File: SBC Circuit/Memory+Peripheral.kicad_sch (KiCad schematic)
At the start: 15 parts, among them U2 68681, U4 MCM6206CP, U5 28C256, U6 MCM6206CP, U7 28C256

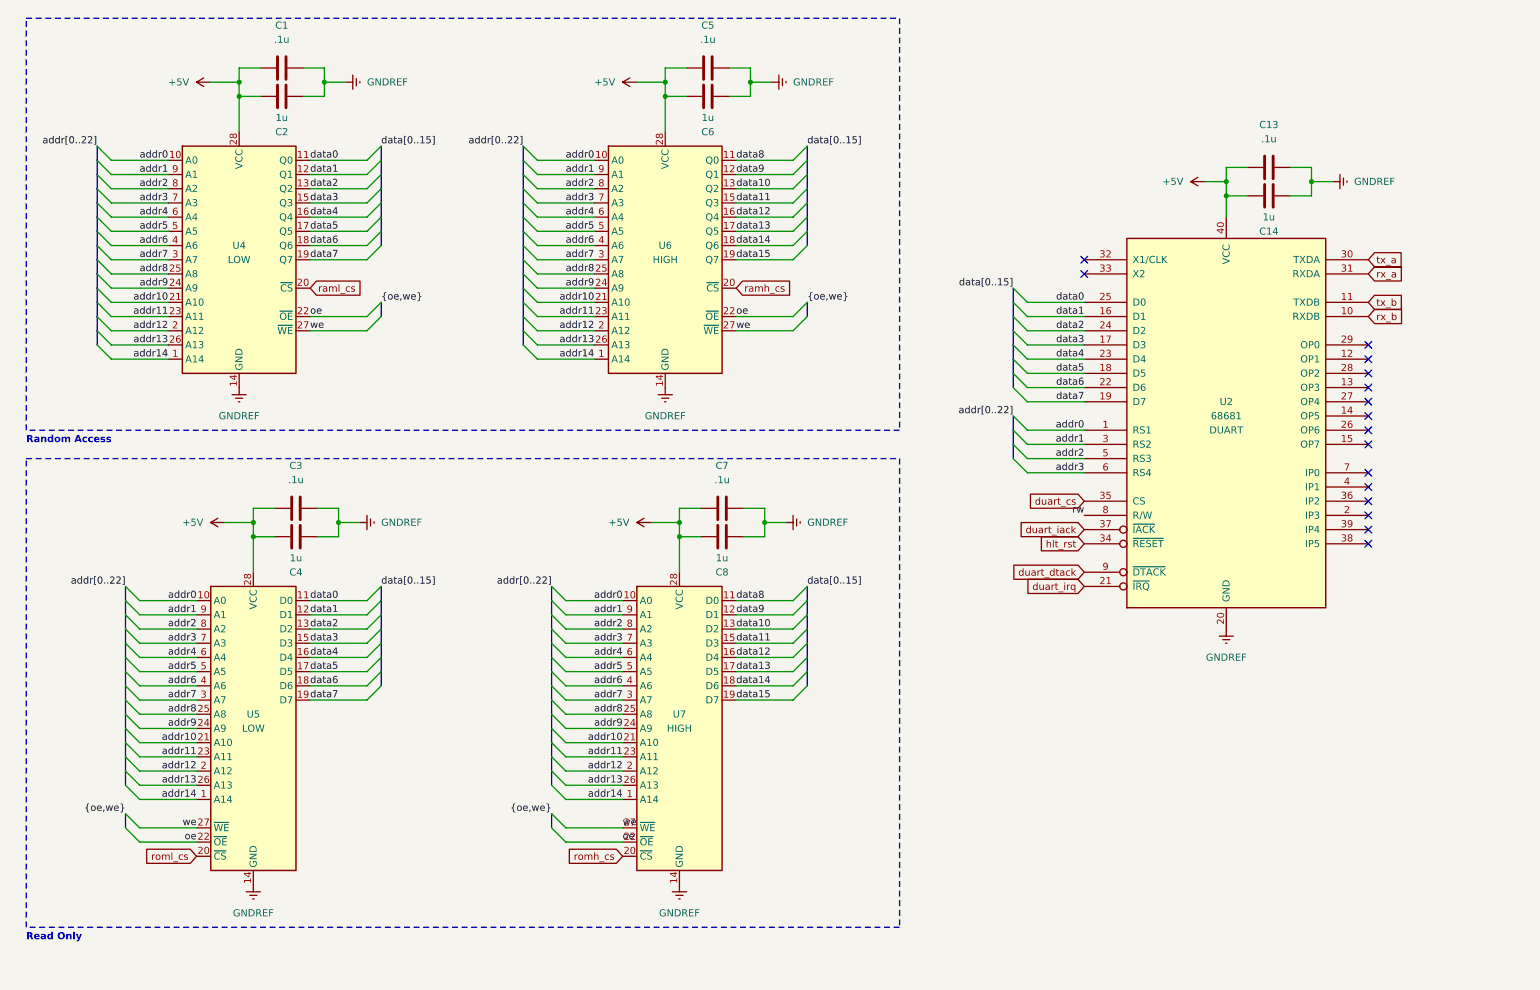
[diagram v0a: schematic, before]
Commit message: Add peripheral headers to schematic
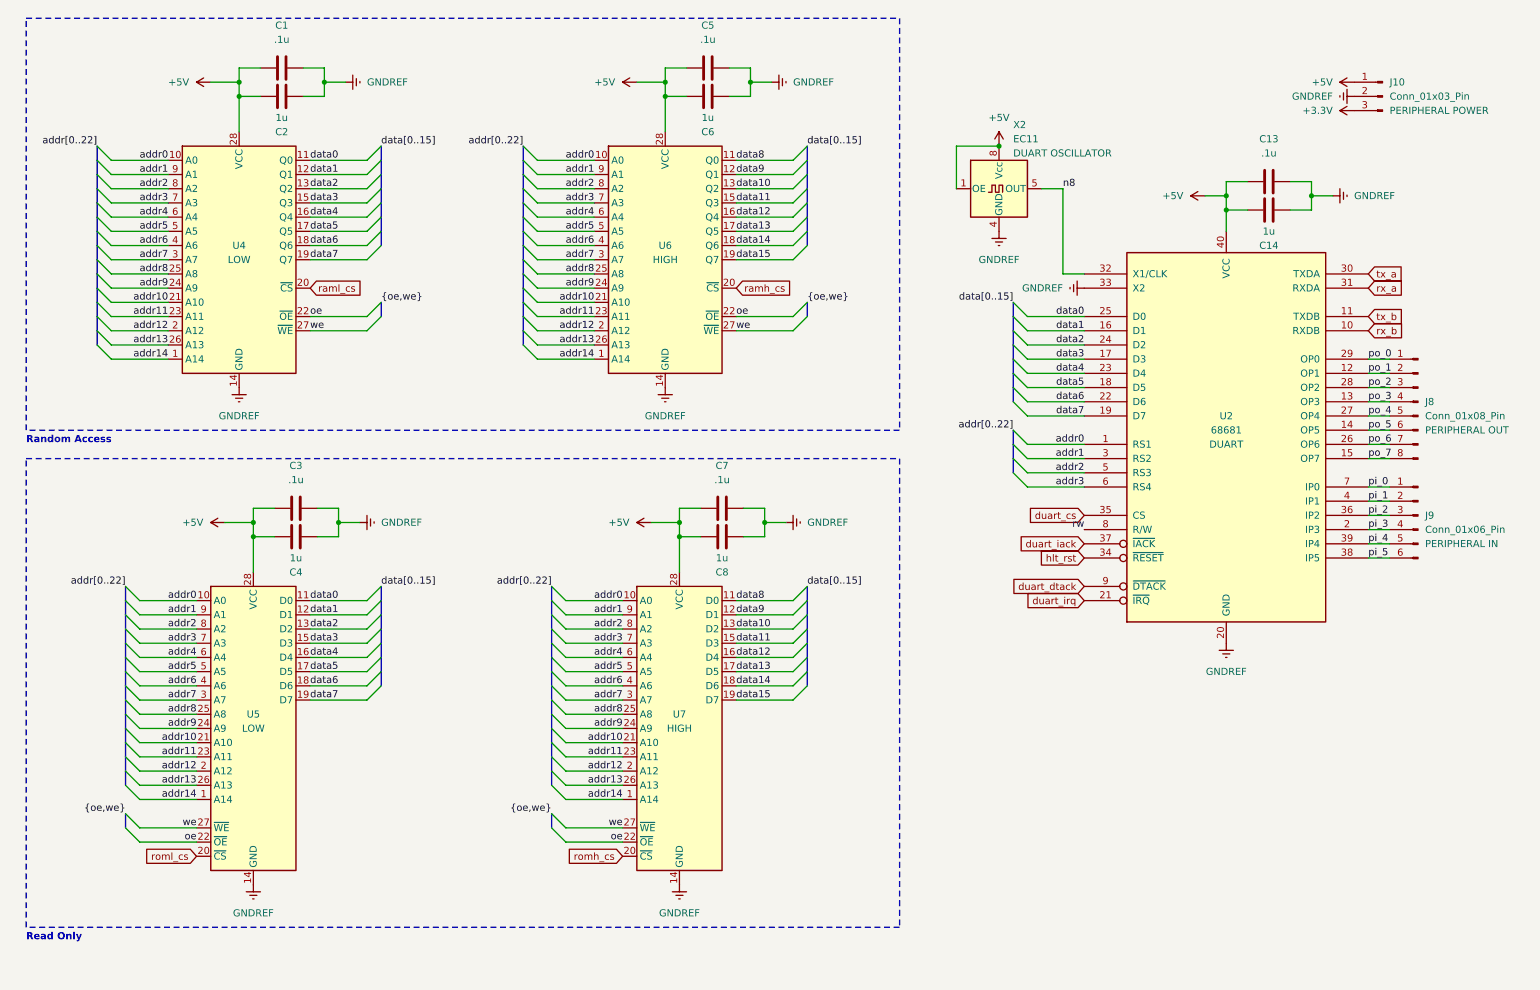
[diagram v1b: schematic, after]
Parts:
- added J10: Conn_01x03_Pin, symbol Connector:Conn_01x03_Pin
- added J8: Conn_01x08_Pin, symbol Connector:Conn_01x08_Pin
- added J9: Conn_01x06_Pin, symbol Connector:Conn_01x06_Pin
- added X2: EC11, Oscillator:Oscillator_SeikoEpson_SG-8002DC, symbol Oscillator:EC11
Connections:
- net +5V: now also J10.1 (Pin_1), X2.1 (OE), X2.8 (Vcc)
- net GNDREF: now also U2.33 (X2), J10.2 (Pin_2), X2.4 (GND)
- net po_1: now reaches U2.12 (OP1)
- net po_1: now also J8.2 (Pin_2)
- net po_3: now reaches U2.13 (OP3)
- net po_3: now also J8.4 (Pin_4)
- net po_5: now reaches U2.14 (OP5)
- net po_5: now also J8.6 (Pin_6)
- net po_7: now reaches U2.15 (OP7)
- net po_7: now also J8.8 (Pin_8)
- net pi_3: now reaches U2.2 (IP3)
- net pi_3: now also J9.4 (Pin_4)
- net po_6: now reaches U2.26 (OP6)
- net po_6: now also J8.7 (Pin_7)
- net po_4: now reaches U2.27 (OP4)
- net po_4: now also J8.5 (Pin_5)
- net po_2: now reaches U2.28 (OP2)
- net po_2: now also J8.3 (Pin_3)
- net po_0: now reaches U2.29 (OP0)
- net po_0: now also J8.1 (Pin_1)
- net n8: now reaches U2.32 (X1/CLK)
- net n8: now also X2.5 (OUT)
- net pi_2: now reaches U2.36 (IP2)
- net pi_2: now also J9.3 (Pin_3)
- net pi_5: now reaches U2.38 (IP5)
- net pi_5: now also J9.6 (Pin_6)
- net pi_4: now reaches U2.39 (IP4)
- net pi_4: now also J9.5 (Pin_5)
- net pi_1: now reaches U2.4 (IP1)
- net pi_1: now also J9.2 (Pin_2)
- net pi_0: now reaches U2.7 (IP0)
- net pi_0: now also J9.1 (Pin_1)
- new net +3.3V: J10.3 (Pin_3)
- no-connect marks 16 -> 0
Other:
- moved on the sheet: C13, C14, U2

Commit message: Reannotate schematic
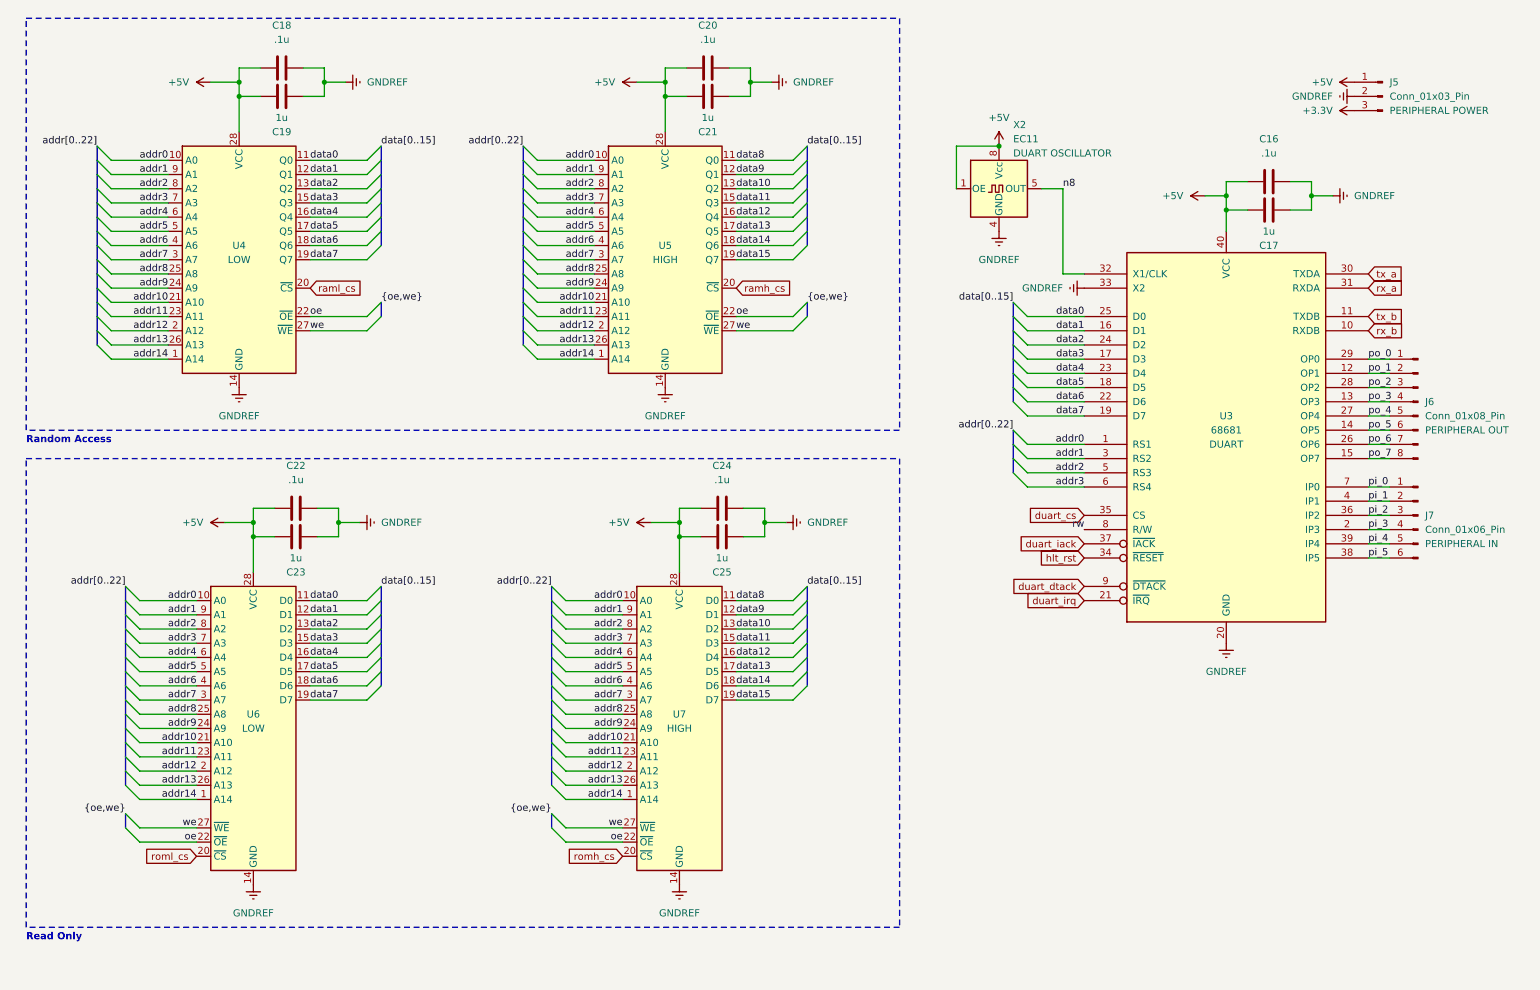
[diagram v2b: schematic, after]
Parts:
- renumbered C13 to C16, C14 to C17, C1 to C18, C2 to C19, C5 to C20, C6 to C21, C3 to C22, C4 to C23, C7 to C24, C8 to C25, J10 to J5, J8 to J6, J9 to J7, U2 to U3, U6 to U5, U5 to U6
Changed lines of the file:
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@@
   (symbol (lib_id "Device:C") (at 64.77 114.3 90) (mirror x) (unit 1)
     (in_bom yes) (on_board yes) (dnp no)
-    (property "Reference" "C4" (at 64.77 120.65 90)
+    (property "Reference" "C23" (at 64.77 120.65 90)
       (effects (font (size 1.27 1.27)))
     )
@@
       (project "SBC Circuit"
         (path "/3db026c4-f98d-4c94-ab2a-d9924b8daebe/58631114-4a93-4344-80be-9965735307cd"
-          (reference "C4") (unit 1)
+          (reference "C23") (unit 1)
         )
       )
@@
   (symbol (lib_id "Device:C") (at 64.77 109.22 90) (unit 1)
     (in_bom yes) (on_board yes) (dnp no) (fields_autoplaced)
-    (property "Reference" "C3" (at 64.77 101.6 90)
+    (property "Reference" "C22" (at 64.77 101.6 90)
       (effects (font (size 1.27 1.27)))
     )
@@
       (project "SBC Circuit"
         (path "/3db026c4-f98d-4c94-ab2a-d9924b8daebe/58631114-4a93-4344-80be-9965735307cd"
-          (reference "C3") (unit 1)
+          (reference "C22") (unit 1)
         )
       )
@@
   (symbol (lib_id "Memory_RAM:MCM6206CP") (at 130.81 64.77 0) (unit 1)
     (in_bom yes) (on_board yes) (dnp no)
-    (property "Reference" "U6" (at 130.81 62.23 0)
+    (property "Reference" "U5" (at 130.81 62.23 0)
       (effects (font (size 1.27 1.27)))
     )
@@
       (project "SBC Circuit"
         (path "/3db026c4-f98d-4c94-ab2a-d9924b8daebe/58631114-4a93-4344-80be-9965735307cd"
-          (reference "U6") (unit 1)
+          (reference "U5") (unit 1)
         )
       )
@@
   (symbol (lib_id "Device:C") (at 238.76 50.8 90) (unit 1)
     (in_bom yes) (on_board yes) (dnp no) (fields_autoplaced)
-    (property "Reference" "C13" (at 238.76 43.18 90)
+    (property "Reference" "C16" (at 238.76 43.18 90)
       (effects (font (size 1.27 1.27)))
     )
@@
       (project "SBC Circuit"
         (path "/3db026c4-f98d-4c94-ab2a-d9924b8daebe/58631114-4a93-4344-80be-9965735307cd"
-          (reference "C13") (unit 1)
+          (reference "C16") (unit 1)
         )
       )
@@
   (symbol (lib_id "Device:C") (at 238.76 55.88 90) (mirror x) (unit 1)
     (in_bom yes) (on_board yes) (dnp no)
-    (property "Reference" "C14" (at 238.76 62.23 90)
+    (property "Reference" "C17" (at 238.76 62.23 90)
       (effects (font (size 1.27 1.27)))
     )
@@
       (project "SBC Circuit"
         (path "/3db026c4-f98d-4c94-ab2a-d9924b8daebe/58631114-4a93-4344-80be-9965735307cd"
-          (reference "C14") (unit 1)
+          (reference "C17") (unit 1)
         )
       )
@@
   (symbol (lib_id "Device:C") (at 62.23 35.56 90) (mirror x) (unit 1)
     (in_bom yes) (on_board yes) (dnp no)
-    (property "Reference" "C2" (at 62.23 41.91 90)
+    (property "Reference" "C19" (at 62.23 41.91 90)
       (effects (font (size 1.27 1.27)))
     )
@@
       (project "SBC Circuit"
         (path "/3db026c4-f98d-4c94-ab2a-d9924b8daebe/58631114-4a93-4344-80be-9965735307cd"
-          (reference "C2") (unit 1)
+          (reference "C19") (unit 1)
         )
       )
@@
   (symbol (lib_id "Device:C") (at 140.97 114.3 90) (mirror x) (unit 1)
     (in_bom yes) (on_board yes) (dnp no)
-    (property "Reference" "C8" (at 140.97 120.65 90)
+    (property "Reference" "C25" (at 140.97 120.65 90)
       (effects (font (size 1.27 1.27)))
     )
@@
       (project "SBC Circuit"
         (path "/3db026c4-f98d-4c94-ab2a-d9924b8daebe/58631114-4a93-4344-80be-9965735307cd"
-          (reference "C8") (unit 1)
+          (reference "C25") (unit 1)
         )
       )
@@
   (symbol (lib_id "Device:C") (at 140.97 109.22 90) (unit 1)
     (in_bom yes) (on_board yes) (dnp no) (fields_autoplaced)
-    (property "Reference" "C7" (at 140.97 101.6 90)
+    (property "Reference" "C24" (at 140.97 101.6 90)
       (effects (font (size 1.27 1.27)))
     )
@@
       (project "SBC Circuit"
         (path "/3db026c4-f98d-4c94-ab2a-d9924b8daebe/58631114-4a93-4344-80be-9965735307cd"
-          (reference "C7") (unit 1)
+          (reference "C24") (unit 1)
         )
       )
@@
   (symbol (lib_id "Device:C") (at 138.43 35.56 90) (mirror x) (unit 1)
     (in_bom yes) (on_board yes) (dnp no)
-    (property "Reference" "C6" (at 138.43 41.91 90)
+    (property "Reference" "C21" (at 138.43 41.91 90)
       (effects (font (size 1.27 1.27)))
     )
@@
       (project "SBC Circuit"
         (path "/3db026c4-f98d-4c94-ab2a-d9924b8daebe/58631114-4a93-4344-80be-9965735307cd"
-          (reference "C6") (unit 1)
+          (reference "C21") (unit 1)
         )
       )
@@
   (symbol (lib_id "Device:C") (at 62.23 30.48 90) (unit 1)
     (in_bom yes) (on_board yes) (dnp no) (fields_autoplaced)
-    (property "Reference" "C1" (at 62.23 22.86 90)
+    (property "Reference" "C18" (at 62.23 22.86 90)
       (effects (font (size 1.27 1.27)))
     )
@@
       (project "SBC Circuit"
         (path "/3db026c4-f98d-4c94-ab2a-d9924b8daebe/58631114-4a93-4344-80be-9965735307cd"
-          (reference "C1") (unit 1)
+          (reference "C18") (unit 1)
         )
       )
@@
   (symbol (lib_id "Connector:Conn_01x03_Pin") (at 259.08 35.56 0) (mirror y) (unit 1)
     (in_bom yes) (on_board yes) (dnp no)
-    (property "Reference" "J10" (at 260.35 33.02 0)
+    (property "Reference" "J5" (at 260.35 33.02 0)
       (effects (font (size 1.27 1.27)) (justify right))
     )
@@
       (project "SBC Circuit"
         (path "/3db026c4-f98d-4c94-ab2a-d9924b8daebe/58631114-4a93-4344-80be-9965735307cd"
-          (reference "J10") (unit 1)
+          (reference "J5") (unit 1)
         )
       )
@@
   (symbol (lib_id "Connector:Conn_01x06_Pin") (at 265.43 110.49 0) (mirror y) (unit 1)
     (in_bom yes) (on_board yes) (dnp no)
-    (property "Reference" "J9" (at 266.7 110.49 0)
+    (property "Reference" "J7" (at 266.7 110.49 0)
       (effects (font (size 1.27 1.27)) (justify right))
     )
@@
       (project "SBC Circuit"
         (path "/3db026c4-f98d-4c94-ab2a-d9924b8daebe/58631114-4a93-4344-80be-9965735307cd"
-          (reference "J9") (unit 1)
+          (reference "J7") (unit 1)
         )
       )
@@
   (symbol (lib_id "Interface:68681") (at 231.14 97.79 0) (unit 1)
     (in_bom yes) (on_board yes) (dnp no)
-    (property "Reference" "U2" (at 231.14 92.71 0)
+    (property "Reference" "U3" (at 231.14 92.71 0)
       (effects (font (size 1.27 1.27)))
     )
@@
       (project "SBC Circuit"
         (path "/3db026c4-f98d-4c94-ab2a-d9924b8daebe/58631114-4a93-4344-80be-9965735307cd"
-          (reference "U2") (unit 1)
+          (reference "U3") (unit 1)
         )
       )
@@
   (symbol (lib_id "Device:C") (at 138.43 30.48 90) (unit 1)
     (in_bom yes) (on_board yes) (dnp no) (fields_autoplaced)
-    (property "Reference" "C5" (at 138.43 22.86 90)
+    (property "Reference" "C20" (at 138.43 22.86 90)
       (effects (font (size 1.27 1.27)))
     )
@@
       (project "SBC Circuit"
         (path "/3db026c4-f98d-4c94-ab2a-d9924b8daebe/58631114-4a93-4344-80be-9965735307cd"
-          (reference "C5") (unit 1)
+          (reference "C20") (unit 1)
         )
       )
@@
   (symbol (lib_id "Connector:Conn_01x08_Pin") (at 265.43 90.17 0) (mirror y) (unit 1)
     (in_bom yes) (on_board yes) (dnp no)
-    (property "Reference" "J8" (at 266.7 90.17 0)
+    (property "Reference" "J6" (at 266.7 90.17 0)
       (effects (font (size 1.27 1.27)) (justify right))
     )
@@
       (project "SBC Circuit"
         (path "/3db026c4-f98d-4c94-ab2a-d9924b8daebe/58631114-4a93-4344-80be-9965735307cd"
-          (reference "J8") (unit 1)
+          (reference "J6") (unit 1)
         )
       )
@@
   (symbol (lib_id "Memory_EEPROM:28C256") (at 57.15 148.59 0) (unit 1)
     (in_bom yes) (on_board yes) (dnp no)
-    (property "Reference" "U5" (at 57.15 146.05 0)
+    (property "Reference" "U6" (at 57.15 146.05 0)
       (effects (font (size 1.27 1.27)))
     )
@@
       (project "SBC Circuit"
         (path "/3db026c4-f98d-4c94-ab2a-d9924b8daebe/58631114-4a93-4344-80be-9965735307cd"
-          (reference "U5") (unit 1)
-        )
-      )
+          (reference "U6") (unit 1)
+        )
+      )
